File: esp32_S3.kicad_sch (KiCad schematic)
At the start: 10 parts, among them SW9 boot, U5 ESP32-S3-WROOM-1, U8 ESP32-S3-DevKitC

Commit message: ESP32S3 push before GPIO label changes
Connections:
- net GPIO0 is gone; now on net GPIO: U5.27 (GPIO0/BOOT), U8.31 (GPIO0)
- net GPIO1 is gone; now on net GPIO: U5.39 (GPIO1/TOUCH1/ADC1_CH0), U8.41 (GPIO1/ADC1_CH0)
- net GPIO10 is gone; now on net GPIO: U5.18 (GPIO10/TOUCH10/ADC1_CH9/FSPICS0/FSPIIO4/SUBSPICS0), U8.16 (GPIO10/ADC1_CH9)
- net GPIO11 is gone; now on net GPIO: U5.19 (GPIO11/TOUCH11/ADC2_CH0/FSPID/FSPIIO5/SUBSPID), U8.17 (GPIO11/ADC2_CH0)
- net GPIO12 is gone; now on net GPIO: U5.20 (GPIO12/TOUCH12/ADC2_CH1/FSPICLK/FSPIIO6/SUBSPICLK), U8.18 (GPIO12/ADC2_CH1)
- net GPIO13 is gone; now on net GPIO: U5.21 (GPIO13/TOUCH13/ADC2_CH2/FSPIQ/FSPIIO7/SUBSPIQ), U8.19 (GPIO13/ADC2_CH2)
- net GPIO14 is gone; now on net GPIO: U5.22 (GPIO14/TOUCH14/ADC2_CH3/FSPIWP/FSPIDQS/SUBSPIWP), U8.20 (GPIO14/ADC2_CH3)
- net GPIO15 is gone; now on net GPIO: U5.8 (GPIO15/U0RTS/ADC2_CH4/XTAL_32K_P), U8.8 (GPIO15/ADC2_CH4/32K_P)
- net GPIO16 is gone; now on net GPIO: U5.9 (GPIO16/U0CTS/ADC2_CH5/XTAL_32K_NH5), U8.9 (GPIO16/ADC2_CH5/32K_N)
- net GPIO17 is gone; now on net GPIO: U5.10 (GPIO17/U1TXD/ADC2_CH6), U8.10 (GPIO17/ADC2_CH6)
- net GPIO18 is gone; now on net GPIO: U5.11 (GPIO18/U1RXD/ADC2_CH7/CLK_OUT3), U8.11 (GPIO18/ADC2_CH7)
- net GPIO2 is gone; now on net GPIO: U5.38 (GPIO2/TOUCH2/ADC1_CH1), U8.40 (GPIO2/ADC1_CH1)
- net GPIO21 is gone; now on net GPIO: U5.23 (GPIO21), U8.27 (GPIO21)
- net GPIO3 is gone; now on net GPIO: U5.15 (GPIO3/TOUCH3/ADC1_CH2), U8.13 (GPIO3/ADC1_CH2)
- net GPIO35 is gone; now on net GPIO: U5.28 (SPIIO6/GPIO35/FSPID/SUBSPID), U8.32 (GPIO35)
- net GPIO36 is gone; now on net GPIO: U5.29 (SPIIO7/GPIO36/FSPICLK/SUBSPICLK), U8.33 (GPIO36)
- net GPIO37 is gone; now on net GPIO: U5.30 (SPIDQS/GPIO37/FSPIQ/SUBSPIQ), U8.34 (GPIO37)
- net GPIO38 is gone; now on net GPIO: U5.31 (GPIO38/FSPIWP/SUBSPIWP), U8.35 (GPIO38)
- net GPIO39 is gone; now on net GPIO: U5.32 (MTCK/GPIO39/CLK_OUT3/SUBSPICS1), U8.36 (GPIO39/MTCK)
- net GPIO4 is gone; now on net GPIO: U5.4 (GPIO4/TOUCH4/ADC1_CH3), U8.4 (GPIO4/ADC1_CH3)
- net GPIO40 is gone; now on net GPIO: U5.33 (MTDO/GPIO40/CLK_OUT2), U8.37 (GPIO40/MTDO)
- net GPIO41 is gone; now on net GPIO: U5.34 (MTDI/GPIO41/CLK_OUT1), U8.38 (GPIO41/MTDI)
- net GPIO42 is gone; now on net GPIO: U5.35 (MTMS/GPIO42), U8.39 (GPIO42/MTMS)
- net GPIO43 is gone; now on net GPIO: U5.37 (U0TXD/GPIO43/CLK_OUT1), U8.43 (GPIO43/U0TXD)
- net GPIO44 is gone; now on net GPIO: U5.36 (U0RXD/GPIO44/CLK_OUT2), U8.42 (GPIO44/U0RXD)
- net GPIO45 is gone; now on net GPIO: U5.26 (GPIO45), U8.30 (GPIO45)
- net GPIO46 is gone; now on net GPIO: U5.16 (GPIO46), U8.14 (GPIO46)
- net GPIO47 is gone; now on net GPIO: U5.24 (GPIO47/SPICLK_P/SUBSPICLK_P_DIFF), U8.28 (GPIO47)
- net GPIO48 is gone; now on net GPIO: U5.25 (GPIO48/SPICLK_N/SUBSPICLK_N_DIFF), U8.29 (GPIO48)
- net GPIO5 is gone; now on net GPIO: U5.5 (GPIO5/TOUCH5/ADC1_CH4), U8.5 (GPIO5/ADC1_CH4)
- net GPIO6 is gone; now on net GPIO: U5.6 (GPIO6/TOUCH6/ADC1_CH5), U8.6 (GPIO6/ADC1_CH5)
- net GPIO7 is gone; now on net GPIO: U5.7 (GPIO7/TOUCH7/ADC1_CH6), U8.7 (GPIO7/ADC1_CH6)
- net GPIO8 is gone; now on net GPIO: U5.12 (GPIO8/TOUCH8/ADC1_CH7/SUBSPICS1), U8.12 (GPIO8/ADC1_CH7)
- net GPIO9 is gone; now on net GPIO: U5.17 (GPIO9/TOUCH9/ADC1_CH8/FSPIHD/SUBSPIHD), U8.15 (GPIO9/ADC1_CH8)
- net EN renamed GPIO

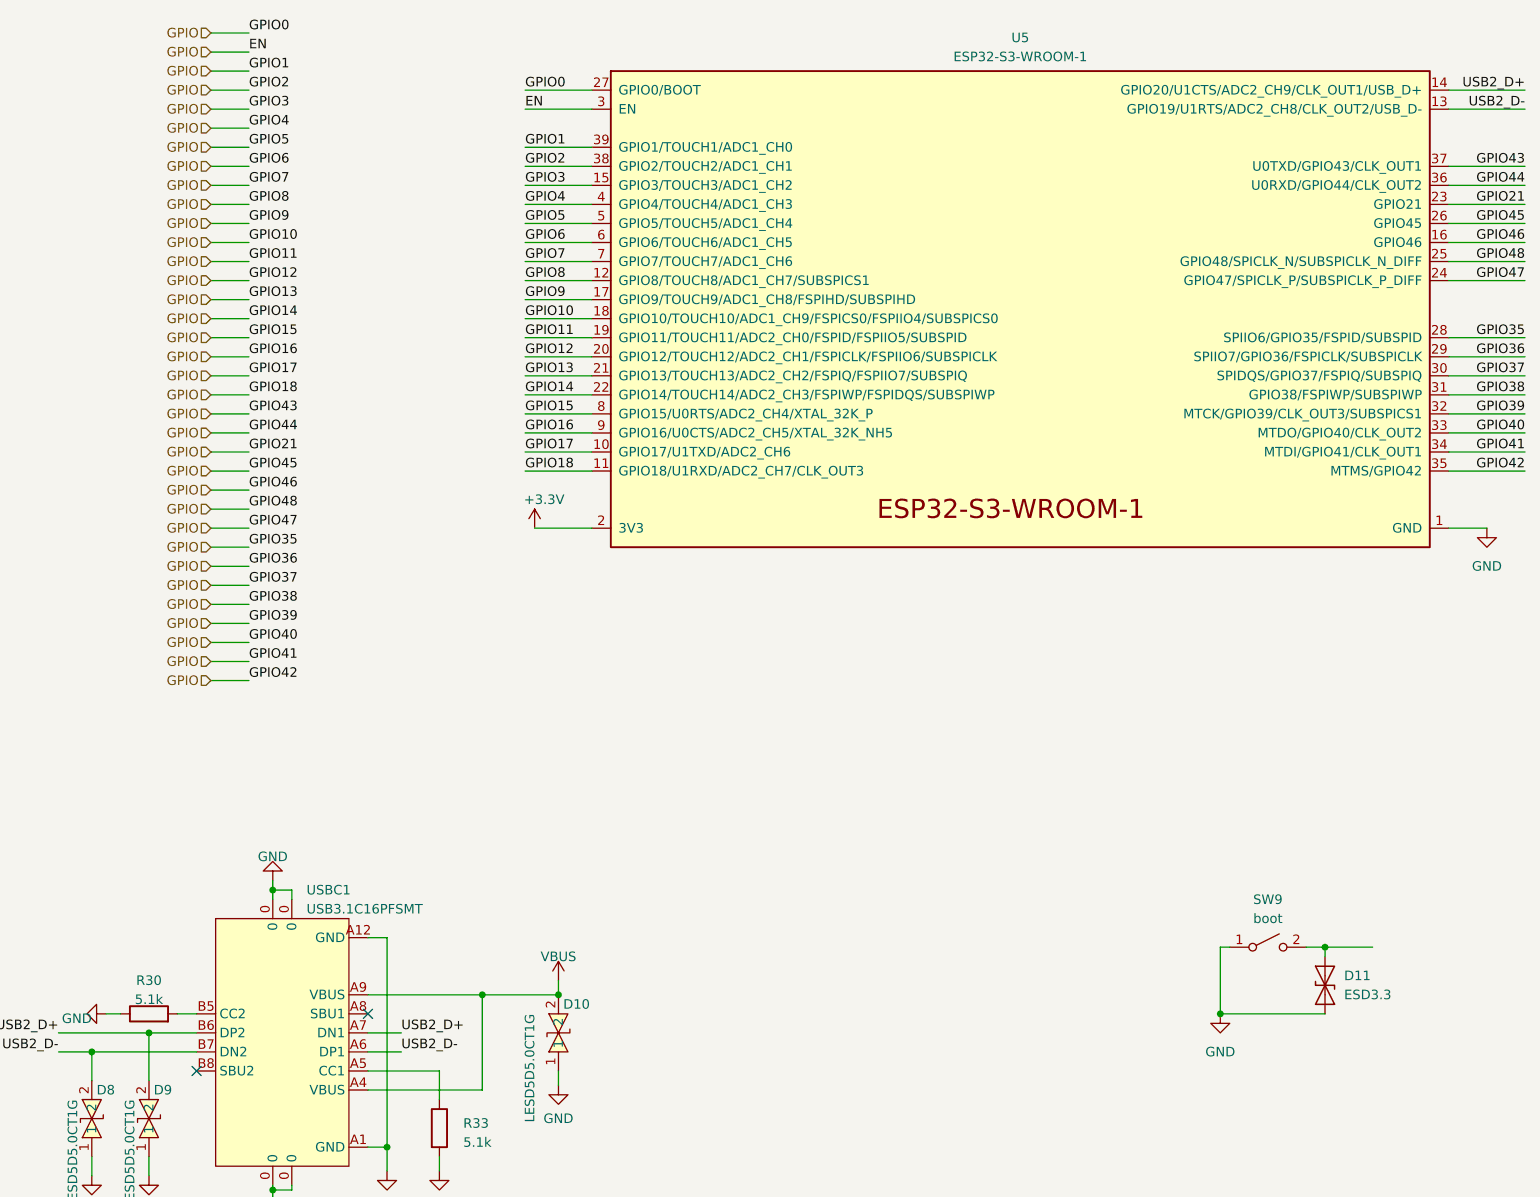
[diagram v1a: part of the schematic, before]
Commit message: ESP32S3: rename hierarchical GPIO labels and remove PCB tracks
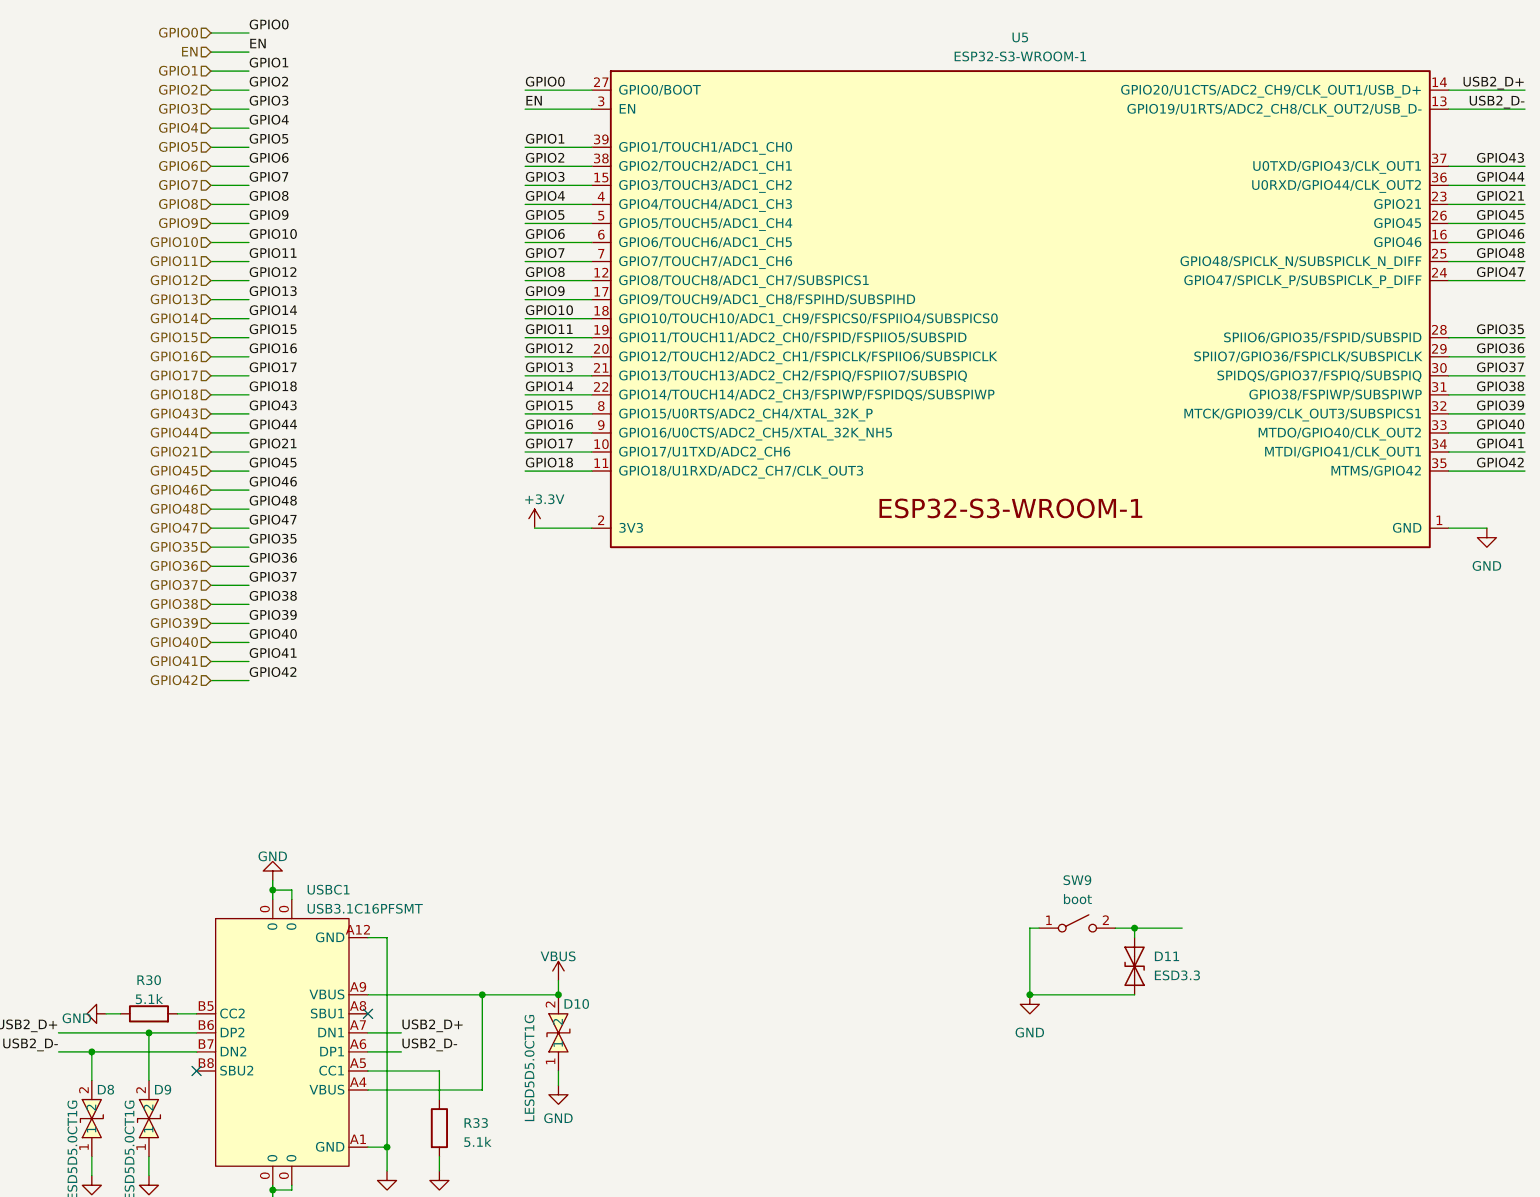
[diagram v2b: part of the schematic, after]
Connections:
- removed net GPIO: U5.10 (GPIO17/U1TXD/ADC2_CH6), U5.11 (GPIO18/U1RXD/ADC2_CH7/CLK_OUT3), U5.12 (GPIO8/TOUCH8/ADC1_CH7/SUBSPICS1), U5.15 (GPIO3/TOUCH3/ADC1_CH2), U5.16 (GPIO46), U5.17 (GPIO9/TOUCH9/ADC1_CH8/FSPIHD/SUBSPIHD), U5.18 (GPIO10/TOUCH10/ADC1_CH9/FSPICS0/FSPIIO4/SUBSPICS0), U5.19 (GPIO11/TOUCH11/ADC2_CH0/FSPID/FSPIIO5/SUBSPID), U5.20 (GPIO12/TOUCH12/ADC2_CH1/FSPICLK/FSPIIO6/SUBSPICLK), U5.21 (GPIO13/TOUCH13/ADC2_CH2/FSPIQ/FSPIIO7/SUBSPIQ), U5.22 (GPIO14/TOUCH14/ADC2_CH3/FSPIWP/FSPIDQS/SUBSPIWP), U5.23 (GPIO21), U5.24 (GPIO47/SPICLK_P/SUBSPICLK_P_DIFF), U5.25 (GPIO48/SPICLK_N/SUBSPICLK_N_DIFF), U5.26 (GPIO45), U5.27 (GPIO0/BOOT), U5.28 (SPIIO6/GPIO35/FSPID/SUBSPID), U5.29 (SPIIO7/GPIO36/FSPICLK/SUBSPICLK), U5.3 (EN), U5.30 (SPIDQS/GPIO37/FSPIQ/SUBSPIQ), U5.31 (GPIO38/FSPIWP/SUBSPIWP), U5.32 (MTCK/GPIO39/CLK_OUT3/SUBSPICS1), U5.33 (MTDO/GPIO40/CLK_OUT2), U5.34 (MTDI/GPIO41/CLK_OUT1), U5.35 (MTMS/GPIO42), U5.36 (U0RXD/GPIO44/CLK_OUT2), U5.37 (U0TXD/GPIO43/CLK_OUT1), U5.38 (GPIO2/TOUCH2/ADC1_CH1), U5.39 (GPIO1/TOUCH1/ADC1_CH0), U5.4 (GPIO4/TOUCH4/ADC1_CH3), U5.5 (GPIO5/TOUCH5/ADC1_CH4), U5.6 (GPIO6/TOUCH6/ADC1_CH5), U5.7 (GPIO7/TOUCH7/ADC1_CH6), U5.8 (GPIO15/U0RTS/ADC2_CH4/XTAL_32K_P), U5.9 (GPIO16/U0CTS/ADC2_CH5/XTAL_32K_NH5), U8.10 (GPIO17/ADC2_CH6), U8.11 (GPIO18/ADC2_CH7), U8.12 (GPIO8/ADC1_CH7), U8.13 (GPIO3/ADC1_CH2), U8.14 (GPIO46), U8.15 (GPIO9/ADC1_CH8), U8.16 (GPIO10/ADC1_CH9), U8.17 (GPIO11/ADC2_CH0), U8.18 (GPIO12/ADC2_CH1), U8.19 (GPIO13/ADC2_CH2), U8.20 (GPIO14/ADC2_CH3), U8.27 (GPIO21), U8.28 (GPIO47), U8.29 (GPIO48), U8.3 (CHIP_PU), U8.30 (GPIO45), U8.31 (GPIO0), U8.32 (GPIO35), U8.33 (GPIO36), U8.34 (GPIO37), U8.35 (GPIO38), U8.36 (GPIO39/MTCK), U8.37 (GPIO40/MTDO), U8.38 (GPIO41/MTDI), U8.39 (GPIO42/MTMS), U8.4 (GPIO4/ADC1_CH3), U8.40 (GPIO2/ADC1_CH1), U8.41 (GPIO1/ADC1_CH0), U8.42 (GPIO44/U0RXD), U8.43 (GPIO43/U0TXD), U8.5 (GPIO5/ADC1_CH4), U8.6 (GPIO6/ADC1_CH5), U8.7 (GPIO7/ADC1_CH6), U8.8 (GPIO15/ADC2_CH4/32K_P), U8.9 (GPIO16/ADC2_CH5/32K_N)
- new net EN: U5.3 (EN), U8.3 (CHIP_PU)
- new net GPIO0: U5.27 (GPIO0/BOOT), U8.31 (GPIO0)
- new net GPIO1: U5.39 (GPIO1/TOUCH1/ADC1_CH0), U8.41 (GPIO1/ADC1_CH0)
- new net GPIO10: U5.18 (GPIO10/TOUCH10/ADC1_CH9/FSPICS0/FSPIIO4/SUBSPICS0), U8.16 (GPIO10/ADC1_CH9)
- new net GPIO11: U5.19 (GPIO11/TOUCH11/ADC2_CH0/FSPID/FSPIIO5/SUBSPID), U8.17 (GPIO11/ADC2_CH0)
- new net GPIO12: U5.20 (GPIO12/TOUCH12/ADC2_CH1/FSPICLK/FSPIIO6/SUBSPICLK), U8.18 (GPIO12/ADC2_CH1)
- new net GPIO13: U5.21 (GPIO13/TOUCH13/ADC2_CH2/FSPIQ/FSPIIO7/SUBSPIQ), U8.19 (GPIO13/ADC2_CH2)
- new net GPIO14: U5.22 (GPIO14/TOUCH14/ADC2_CH3/FSPIWP/FSPIDQS/SUBSPIWP), U8.20 (GPIO14/ADC2_CH3)
- new net GPIO15: U5.8 (GPIO15/U0RTS/ADC2_CH4/XTAL_32K_P), U8.8 (GPIO15/ADC2_CH4/32K_P)
- new net GPIO16: U5.9 (GPIO16/U0CTS/ADC2_CH5/XTAL_32K_NH5), U8.9 (GPIO16/ADC2_CH5/32K_N)
- new net GPIO17: U5.10 (GPIO17/U1TXD/ADC2_CH6), U8.10 (GPIO17/ADC2_CH6)
- new net GPIO18: U5.11 (GPIO18/U1RXD/ADC2_CH7/CLK_OUT3), U8.11 (GPIO18/ADC2_CH7)
- new net GPIO2: U5.38 (GPIO2/TOUCH2/ADC1_CH1), U8.40 (GPIO2/ADC1_CH1)
- new net GPIO21: U5.23 (GPIO21), U8.27 (GPIO21)
- new net GPIO3: U5.15 (GPIO3/TOUCH3/ADC1_CH2), U8.13 (GPIO3/ADC1_CH2)
- new net GPIO35: U5.28 (SPIIO6/GPIO35/FSPID/SUBSPID), U8.32 (GPIO35)
- new net GPIO36: U5.29 (SPIIO7/GPIO36/FSPICLK/SUBSPICLK), U8.33 (GPIO36)
- new net GPIO37: U5.30 (SPIDQS/GPIO37/FSPIQ/SUBSPIQ), U8.34 (GPIO37)
- new net GPIO38: U5.31 (GPIO38/FSPIWP/SUBSPIWP), U8.35 (GPIO38)
- new net GPIO39: U5.32 (MTCK/GPIO39/CLK_OUT3/SUBSPICS1), U8.36 (GPIO39/MTCK)
- new net GPIO4: U5.4 (GPIO4/TOUCH4/ADC1_CH3), U8.4 (GPIO4/ADC1_CH3)
- new net GPIO40: U5.33 (MTDO/GPIO40/CLK_OUT2), U8.37 (GPIO40/MTDO)
- new net GPIO41: U5.34 (MTDI/GPIO41/CLK_OUT1), U8.38 (GPIO41/MTDI)
- new net GPIO42: U5.35 (MTMS/GPIO42), U8.39 (GPIO42/MTMS)
- new net GPIO43: U5.37 (U0TXD/GPIO43/CLK_OUT1), U8.43 (GPIO43/U0TXD)
- new net GPIO44: U5.36 (U0RXD/GPIO44/CLK_OUT2), U8.42 (GPIO44/U0RXD)
- new net GPIO45: U5.26 (GPIO45), U8.30 (GPIO45)
- new net GPIO46: U5.16 (GPIO46), U8.14 (GPIO46)
- new net GPIO47: U5.24 (GPIO47/SPICLK_P/SUBSPICLK_P_DIFF), U8.28 (GPIO47)
- new net GPIO48: U5.25 (GPIO48/SPICLK_N/SUBSPICLK_N_DIFF), U8.29 (GPIO48)
- new net GPIO5: U5.5 (GPIO5/TOUCH5/ADC1_CH4), U8.5 (GPIO5/ADC1_CH4)
- new net GPIO6: U5.6 (GPIO6/TOUCH6/ADC1_CH5), U8.6 (GPIO6/ADC1_CH5)
- new net GPIO7: U5.7 (GPIO7/TOUCH7/ADC1_CH6), U8.7 (GPIO7/ADC1_CH6)
- new net GPIO8: U5.12 (GPIO8/TOUCH8/ADC1_CH7/SUBSPICS1), U8.12 (GPIO8/ADC1_CH7)
- new net GPIO9: U5.17 (GPIO9/TOUCH9/ADC1_CH8/FSPIHD/SUBSPIHD), U8.15 (GPIO9/ADC1_CH8)
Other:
- moved on the sheet: D11, SW9
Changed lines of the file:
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@@
 	)
 	(junction
-		(at 344.17 217.17)
+		(at 318.77 214.63)
 		(diameter 0)
 		(color 0 0 0 0)
@@
 	)
 	(junction
-		(at 330.2 226.06)
+		(at 304.8 223.52)
 		(diameter 0)
 		(color 0 0 0 0)
@@
 	(wire
 		(pts
-			(xy 344.17 217.17) (xy 350.52 217.17)
+			(xy 318.77 214.63) (xy 325.12 214.63)
 		)
 		(stroke
@@
 	(wire
 		(pts
-			(xy 341.63 217.17) (xy 344.17 217.17)
+			(xy 316.23 214.63) (xy 318.77 214.63)
 		)
 		(stroke
@@
 	(wire
 		(pts
-			(xy 330.2 226.06) (xy 344.17 226.06)
+			(xy 304.8 223.52) (xy 318.77 223.52)
 		)
 		(stroke
@@
 	(wire
 		(pts
-			(xy 330.2 217.17) (xy 330.2 226.06)
+			(xy 304.8 214.63) (xy 304.8 223.52)
 		)
 		(stroke
@@
 	(wire
 		(pts
-			(xy 344.17 217.17) (xy 344.17 218.44)
+			(xy 318.77 214.63) (xy 318.77 215.9)
 		)
 		(stroke
@@
 	(wire
 		(pts
-			(xy 331.47 217.17) (xy 330.2 217.17)
+			(xy 306.07 214.63) (xy 304.8 214.63)
 		)
 		(stroke
@@
 		)
 	)
-	(hierarchical_label "GPIO"
+	(hierarchical_label "GPIO1"
 		(shape input)
 		(at 195.58 100.33 180)
@@
 		)
 	)
-	(hierarchical_label "GPIO"
+	(hierarchical_label "GPIO0"
 		(shape input)
 		(at 195.58 95.25 180)
@@
 		)
 	)
-	(hierarchical_label "GPIO"
+	(hierarchical_label "GPIO18"
 		(shape input)
 		(at 195.58 143.51 180)
@@
 		)
 	)
-	(hierarchical_label "GPIO"
+	(hierarchical_label "GPIO4"
 		(shape input)
 		(at 195.58 107.95 180)
@@
 		)
 	)
-	(hierarchical_label "GPIO"
+	(hierarchical_label "GPIO43"
 		(shape input)
 		(at 195.58 146.05 180)
@@
 		)
 	)
-	(hierarchical_label "GPIO"
+	(hierarchical_label "GPIO15"
 		(shape input)
 		(at 195.58 135.89 180)
@@
 		)
 	)
-	(hierarchical_label "GPIO"
+	(hierarchical_label "GPIO14"
 		(shape input)
 		(at 195.58 133.35 180)
@@
 		)
 	)
-	(hierarchical_label "GPIO"
+	(hierarchical_label "GPIO10"
 		(shape input)
 		(at 195.58 123.19 180)
@@
 		)
 	)
-	(hierarchical_label "GPIO"
+	(hierarchical_label "GPIO17"
 		(shape input)
 		(at 195.58 140.97 180)
@@
 		)
 	)
-	(hierarchical_label "GPIO"
+	(hierarchical_label "GPIO16"
 		(shape input)
 		(at 195.58 138.43 180)
@@
 		)
 	)
-	(hierarchical_label "GPIO"
+	(hierarchical_label "GPIO37"
 		(shape input)
 		(at 195.58 168.91 180)
@@
 		)
 	)
-	(hierarchical_label "GPIO"
+	(hierarchical_label "GPIO47"
 		(shape input)
 		(at 195.58 161.29 180)
@@
 		)
 	)
-	(hierarchical_label "GPIO"
+	(hierarchical_label "GPIO44"
 		(shape input)
 		(at 195.58 148.59 180)
@@
 		)
 	)
-	(hierarchical_label "GPIO"
+	(hierarchical_label "GPIO7"
 		(shape input)
 		(at 195.58 115.57 180)
@@
 		)
 	)
-	(hierarchical_label "GPIO"
+	(hierarchical_label "GPIO38"
 		(shape input)
 		(at 195.58 171.45 180)
@@
 		)
 	)
-	(hierarchical_label "GPIO"
+	(hierarchical_label "GPIO2"
 		(shape input)
 		(at 195.58 102.87 180)
@@
 		)
 	)
-	(hierarchical_label "GPIO"
+	(hierarchical_label "GPIO21"
 		(shape input)
 		(at 195.58 151.13 180)
@@
 		)
 	)
-	(hierarchical_label "GPIO"
+	(hierarchical_label "GPIO40"
 		(shape input)
 		(at 195.58 176.53 180)
@@
 		)
 	)
-	(hierarchical_label "GPIO"
+	(hierarchical_label "GPIO41"
 		(shape input)
 		(at 195.58 179.07 180)
@@
 		)
 	)
-	(hierarchical_label "GPIO"
+	(hierarchical_label "GPIO42"
 		(shape input)
 		(at 195.58 181.61 180)
@@
 		)
 	)
-	(hierarchical_label "GPIO"
+	(hierarchical_label "GPIO12"
 		(shape input)
 		(at 195.58 128.27 180)
@@
 		)
 	)
-	(hierarchical_label "GPIO"
+	(hierarchical_label "GPIO5"
 		(shape input)
 		(at 195.58 110.49 180)
@@
 		)
 	)
-	(hierarchical_label "GPIO"
+	(hierarchical_label "GPIO48"
 		(shape input)
 		(at 195.58 158.75 180)
@@
 		)
 	)
-	(hierarchical_label "GPIO"
+	(hierarchical_label "GPIO3"
 		(shape input)
 		(at 195.58 105.41 180)
@@
 		)
 	)
-	(hierarchical_label "GPIO"
+	(hierarchical_label "GPIO39"
 		(shape input)
 		(at 195.58 173.99 180)
@@
 		)
 	)
-	(hierarchical_label "GPIO"
+	(hierarchical_label "GPIO13"
 		(shape input)
 		(at 195.58 130.81 180)
@@
 		)
 	)
-	(hierarchical_label "GPIO"
+	(hierarchical_label "GPIO6"
 		(shape input)
 		(at 195.58 113.03 180)
@@
 		)
 	)
-	(hierarchical_label "GPIO"
+	(hierarchical_label "GPIO9"
 		(shape input)
 		(at 195.58 120.65 180)
@@
 		)
 	)
-	(hierarchical_label "GPIO"
+	(hierarchical_label "GPIO35"
 		(shape input)
 		(at 195.58 163.83 180)
@@
 		)
 	)
-	(hierarchical_label "GPIO"
+	(hierarchical_label "GPIO46"
 		(shape input)
 		(at 195.58 156.21 180)
@@
 		)
 	)
-	(hierarchical_label "GPIO"
+	(hierarchical_label "GPIO36"
 		(shape input)
 		(at 195.58 166.37 180)
@@
 		)
 	)
-	(hierarchical_label "GPIO"
+	(hierarchical_label "EN"
 		(shape input)
 		(at 195.58 97.79 180)
@@
 		)
 	)
-	(hierarchical_label "GPIO"
+	(hierarchical_label "GPIO45"
 		(shape input)
 		(at 195.58 153.67 180)
@@
 		)
 	)
-	(hierarchical_label "GPIO"
+	(hierarchical_label "GPIO11"
 		(shape input)
 		(at 195.58 125.73 180)
@@
 		)
 	)
-	(hierarchical_label "GPIO"
+	(hierarchical_label "GPIO8"
 		(shape input)
 		(at 195.58 118.11 180)
@@
 	(symbol
 		(lib_id "power:GND")
-		(at 330.2 226.06 0)
+		(at 304.8 223.52 0)
 		(unit 1)
 		(body_style 1)
@@
 		(fields_autoplaced yes)
 		(property "Reference" "#PWR074"
-			(at 330.2 232.41 0)
+			(at 304.8 229.87 0)
 			(hide yes)
 			(show_name no)
@@
 		)
 		(property "Value" "GND"
-			(at 330.2 231.14 0)
+			(at 304.8 228.6 0)
 			(show_name no)
 			(do_not_autoplace no)
@@
 		)
 		(property "Footprint" ""
-			(at 330.2 226.06 0)
+			(at 304.8 223.52 0)
 			(hide yes)
 			(show_name no)
@@
 		)
 		(property "Datasheet" ""
-			(at 330.2 226.06 0)
+			(at 304.8 223.52 0)
 			(hide yes)
 			(show_name no)
@@
 		)
 		(property "Description" "Power symbol creates a global label with name \"GND\" , ground"
-			(at 330.2 226.06 0)
+			(at 304.8 223.52 0)
 			(hide yes)
 			(show_name no)
@@
 	(symbol
 		(lib_id "Diode:ESD9B3.3ST5G")
-		(at 344.17 222.25 90)
+		(at 318.77 219.71 90)
 		(unit 1)
 		(body_style 1)
@@
 		(fields_autoplaced yes)
 		(property "Reference" "D11"
-			(at 346.71 220.9799 90)
+			(at 321.31 218.4399 90)
 			(show_name no)
 			(do_not_autoplace no)
@@
 		)
 		(property "Value" "ESD3.3"
-			(at 346.71 223.5199 90)
+			(at 321.31 220.9799 90)
 			(show_name no)
 			(do_not_autoplace no)
@@
 		)
 		(property "Footprint" "Diode_SMD:D_SOD-923"
-			(at 344.17 222.25 0)
+			(at 318.77 219.71 0)
 			(hide yes)
 			(show_name no)
@@
 		)
 		(property "Datasheet" "https://www.onsemi.com/pub/Collateral/ESD9B-D.PDF"
-			(at 344.17 222.25 0)
+			(at 318.77 219.71 0)
 			(hide yes)
 			(show_name no)
@@
 		)
 		(property "Description" "ESD protection diode, 3.3Vrwm, SOD-923"
-			(at 344.17 222.25 0)
+			(at 318.77 219.71 0)
 			(hide yes)
 			(show_name no)
@@
 	(symbol
 		(lib_id "Switch:SW_SPST")
-		(at 336.55 217.17 0)
+		(at 311.15 214.63 0)
 		(unit 1)
 		(body_style 1)
@@
 		(fields_autoplaced yes)
 		(property "Reference" "SW9"
-			(at 336.55 210.82 0)
+			(at 311.15 208.28 0)
 			(show_name no)
 			(do_not_autoplace no)
@@
 		)
 		(property "Value" "boot"
-			(at 336.55 213.36 0)
+			(at 311.15 210.82 0)
 			(show_name no)
 			(do_not_autoplace no)
@@
 		)
 		(property "Footprint" "Button_Switch_SMD:SW_SPST_B3U-1000P"
-			(at 336.55 217.17 0)
+			(at 311.15 214.63 0)
 			(hide yes)
 			(show_name no)
@@
 		)
 		(property "Datasheet" ""
-			(at 336.55 217.17 0)
+			(at 311.15 214.63 0)
 			(hide yes)
 			(show_name no)
@@
 		)
 		(property "Description" "Single Pole Single Throw (SPST) switch"
-			(at 336.55 217.17 0)
+			(at 311.15 214.63 0)
 			(hide yes)
 			(show_name no)

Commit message: Actualización de esquemáticos y PCB
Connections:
- net USB2_D+ renamed GPIO20
- net USB2_D- renamed GPIO19
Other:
- moved on the sheet: D11, SW9, U8
